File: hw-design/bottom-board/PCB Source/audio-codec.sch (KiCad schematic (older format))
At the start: 36 parts, among them U5 AP2120N-3.3, U6 CS4265, X1 24.576MHz

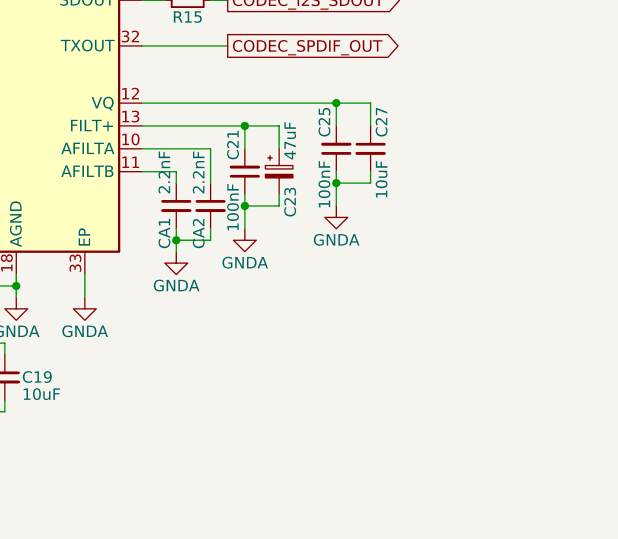
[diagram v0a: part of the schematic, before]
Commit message: change bias voltages to 5V, isolate input GND connections
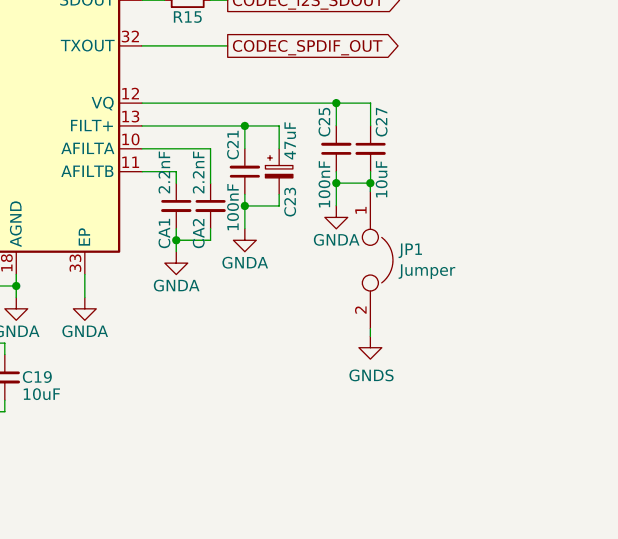
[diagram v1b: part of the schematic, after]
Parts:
- added JP1: Jumper, Jumper:SolderJumper-2_P1.3mm_Bridged_Pad1.0x1.5mm, symbol Device:Jumper
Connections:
- net GNDA: now also JP1.1
- new net GNDS: JP1.2
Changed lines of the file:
@@
 	7650 4400 7650 4450
 Wire Wire Line
-	7650 4450 7500 4450
+	7650 4450 7649 4450
 Connection ~ 7500 4450
 Wire Wire Line
@@
 Text Notes 3025 5625 0    60   ~ 0
 The series resistor at I2S_MCLK \nmust only be placed when the xtal\nis not placed, and vice versa.
+$Comp
+L power:GNDS #PWR0207
+U 1 1 5FE9F786
+P 7649 5120
+F 0 "#PWR0207" H 7649 4870 50  0001 C CNN
+F 1 "GNDS" H 7654 4947 50  0000 C CNN
+F 2 "" H 7649 5120 50  0001 C CNN
+F 3 "" H 7649 5120 50  0001 C CNN
+	1    7649 5120
+	1    0    0    -1
+$EndComp
+$Comp
+L Device:Jumper JP1
+U 1 1 5FEA81D1
+P 7649 4787
+F 0 "JP1" V 7603 4914 50  0000 L CNN
+F 1 "Jumper" V 7694 4914 50  0000 L CNN
+F 2 "Jumper:SolderJumper-2_P1.3mm_Bridged_Pad1.0x1.5mm" H 7649 4787 50  0001 C CNN
+F 3 "~" H 7649 4787 50  0001 C CNN
+	1    7649 4787
+	0    1    1    0
+$EndComp
+Wire Wire Line
+	7649 4487 7649 4450
+Connection ~ 7649 4450
+Wire Wire Line
+	7649 4450 7500 4450
+Wire Wire Line
+	7649 5087 7649 5120
 $EndSCHEMATC

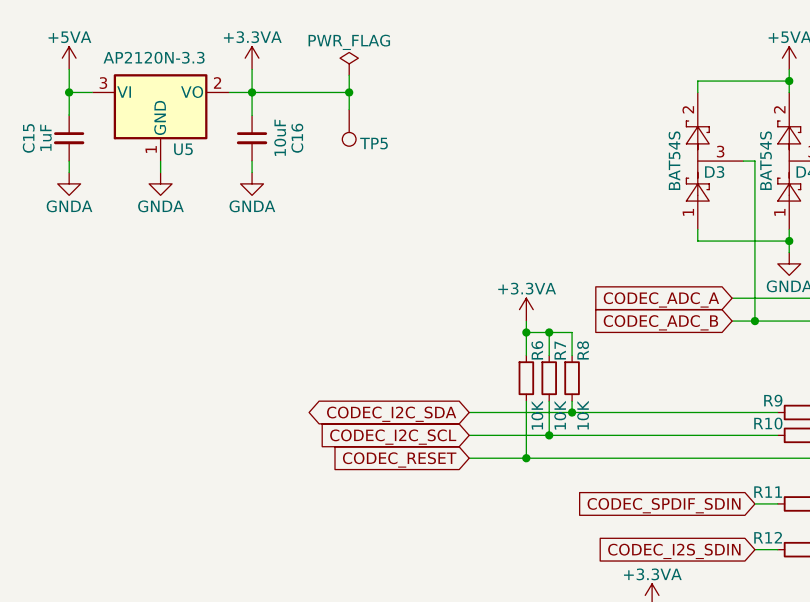
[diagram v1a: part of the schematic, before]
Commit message: add docs + change pwr schematic
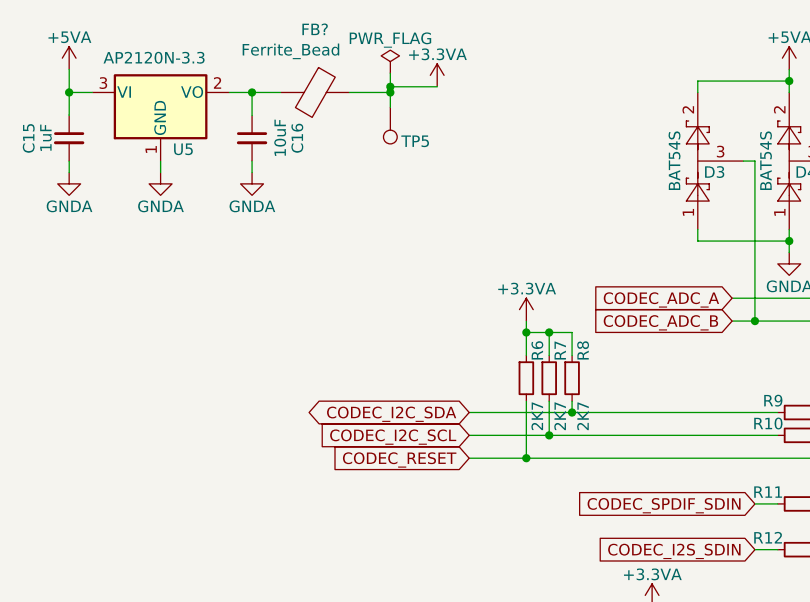
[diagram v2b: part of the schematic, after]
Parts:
- added FB?: Ferrite_Bead, symbol Device:Ferrite_Bead
- R6, R7, R8: value 10K -> 2K7; MPN RR0816P-103-D -> (none)
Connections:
- net +3.3VA: now also FB?.1; no longer C16.1, U5.2 (VO)
- new net: C16.1, FB?.2, U5.2 (VO)
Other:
- moved on the sheet: TP5
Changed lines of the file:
@@
 L bottom-board-rescue:+3.3VA-power #PWR038
 U 1 1 5B50883D
-P 2500 1950
-F 0 "#PWR038" H 2500 1800 50  0001 C CNN
-F 1 "+3.3VA" H 2500 2090 50  0000 C CNN
-F 2 "" H 2500 1950 50  0001 C CNN
-F 3 "" H 2500 1950 50  0001 C CNN
-	1    2500 1950
+P 3310 2025
+F 0 "#PWR038" H 3310 1875 50  0001 C CNN
+F 1 "+3.3VA" H 3310 2165 50  0000 C CNN
+F 2 "" H 3310 2025 50  0001 C CNN
+F 3 "" H 3310 2025 50  0001 C CNN
+	1    3310 2025
 	1    0    0    -1
 $EndComp
@@
 Connection ~ 1700 2050
 Wire Wire Line
-	2500 1950 2500 2050
-Wire Wire Line
 	2400 2050 2500 2050
-Connection ~ 2500 2050
 $Comp
 L bottom-board-rescue:GNDA-power #PWR039
@@
 L bottom-board-rescue:PWR_FLAG-power #FLG04
 U 1 1 5B621D3C
-P 2925 1975
-F 0 "#FLG04" H 2925 2050 50  0001 C CNN
-F 1 "PWR_FLAG" H 2925 2125 50  0000 C CNN
-F 2 "" H 2925 1975 50  0001 C CNN
-F 3 "~" H 2925 1975 50  0001 C CNN
-	1    2925 1975
-	1    0    0    -1
-$EndComp
-Wire Wire Line
-	2925 1975 2925 2050
-Wire Wire Line
-	2925 2050 2500 2050
+P 3105 1965
+F 0 "#FLG04" H 3105 2040 50  0001 C CNN
+F 1 "PWR_FLAG" H 3105 2115 50  0000 C CNN
+F 2 "" H 3105 1965 50  0001 C CNN
+F 3 "~" H 3105 1965 50  0001 C CNN
+	1    3105 1965
+	1    0    0    -1
+$EndComp
 $Comp
 L bottom-board-rescue:C_Small-Device C?
@@
 AR Path="/54F72B97/5B7E4010" Ref="R6"  Part="1"
 F 0 "R6" V 3750 3375 50  0000 L CNN
-F 1 "10K" V 3750 3200 50  0000 R CNN
+F 1 "2K7" V 3750 3200 50  0000 R CNN
 F 2 "Resistor_SMD:R_0603_1608Metric" H 3700 3300 60  0001 C CNN
 F 3 "" H 3700 3300 60  0000 C CNN
-F 4 "RR0816P-103-D" H 1950 -3350 50  0001 C CNN "MPN"
+F 4 "" H 1950 -3350 50  0001 C CNN "MPN"
 	1    3700 3300
 	1    0    0    -1
@@
 AR Path="/54F72B97/5B7EA59F" Ref="R7"  Part="1"
 F 0 "R7" V 3850 3375 50  0000 L CNN
-F 1 "10K" V 3850 3200 50  0000 R CNN
+F 1 "2K7" V 3850 3200 50  0000 R CNN
 F 2 "Resistor_SMD:R_0603_1608Metric" H 3800 3300 60  0001 C CNN
 F 3 "" H 3800 3300 60  0000 C CNN
-F 4 "RR0816P-103-D" H 2050 -3350 50  0001 C CNN "MPN"
+F 4 "" H 2050 -3350 50  0001 C CNN "MPN"
 	1    3800 3300
 	1    0    0    -1
@@
 AR Path="/54F72B97/5B7EA603" Ref="R8"  Part="1"
 F 0 "R8" V 3950 3375 50  0000 L CNN
-F 1 "10K" V 3950 3200 50  0000 R CNN
+F 1 "2K7" V 3950 3200 50  0000 R CNN
 F 2 "Resistor_SMD:R_0603_1608Metric" H 3900 3300 60  0001 C CNN
 F 3 "" H 3900 3300 60  0000 C CNN
-F 4 "RR0816P-103-D" H 2150 -3350 50  0001 C CNN "MPN"
 	1    3900 3300
 	1    0    0    -1
@@
 L bottom-board-rescue:TestPoint-Connector TP?
 U 1 1 5BCC4F8F
-P 2925 2125
+P 3105 2115
 AR Path="/54F7244B/5BCC4F8F" Ref="TP?"  Part="1"
 AR Path="/54F72B97/5BCC4F8F" Ref="TP5"  Part="1"
-F 0 "TP5" H 2750 2275 50  0000 L CNN
-F 1 "TestPoint" H 2983 2154 50  0001 L CNN
-F 2 "TestPoint:TestPoint_Pad_D1.0mm" H 3125 2125 50  0001 C CNN
-F 3 "~" H 3125 2125 50  0001 C CNN
-	1    2925 2125
-	-1   0    0    1
-$EndComp
-Wire Wire Line
-	2925 2125 2925 2050
-Connection ~ 2925 2050
+F 0 "TP5" H 2930 2265 50  0000 L CNN
+F 1 "TestPoint" H 3163 2144 50  0001 L CNN
+F 2 "TestPoint:TestPoint_Pad_D1.0mm" H 3305 2115 50  0001 C CNN
+F 3 "~" H 3305 2115 50  0001 C CNN
+	1    3105 2115
+	-1   0    0    1
+$EndComp
 $Comp
 L bottom-board-rescue:R_Small-Device R19
@@
 Wire Wire Line
 	7649 5087 7649 5120
+$Comp
+L Device:Ferrite_Bead FB?
+U 1 1 618FF74E
+P 2775 2050
+F 0 "FB?" V 2501 2050 50  0000 C CNN
+F 1 "Ferrite_Bead" V 2590 1945 50  0000 C CNN
+F 2 "" V 2705 2050 50  0001 C CNN
+F 3 "~" H 2775 2050 50  0001 C CNN
+	1    2775 2050
+	0    1    1    0
+$EndComp
+Wire Wire Line
+	3310 2025 3105 2025
+Wire Wire Line
+	3105 1965 3105 2025
+Wire Wire Line
+	3105 2115 3105 2050
+Connection ~ 3105 2025
+Wire Wire Line
+	2625 2050 2500 2050
+Connection ~ 2500 2050
+Wire Wire Line
+	2925 2050 3105 2050
+Wire Wire Line
+	3105 2050 3105 2025
+Connection ~ 3105 2050
+Wire Wire Line
+	3105 2050 3105 2025
 $EndSCHEMATC

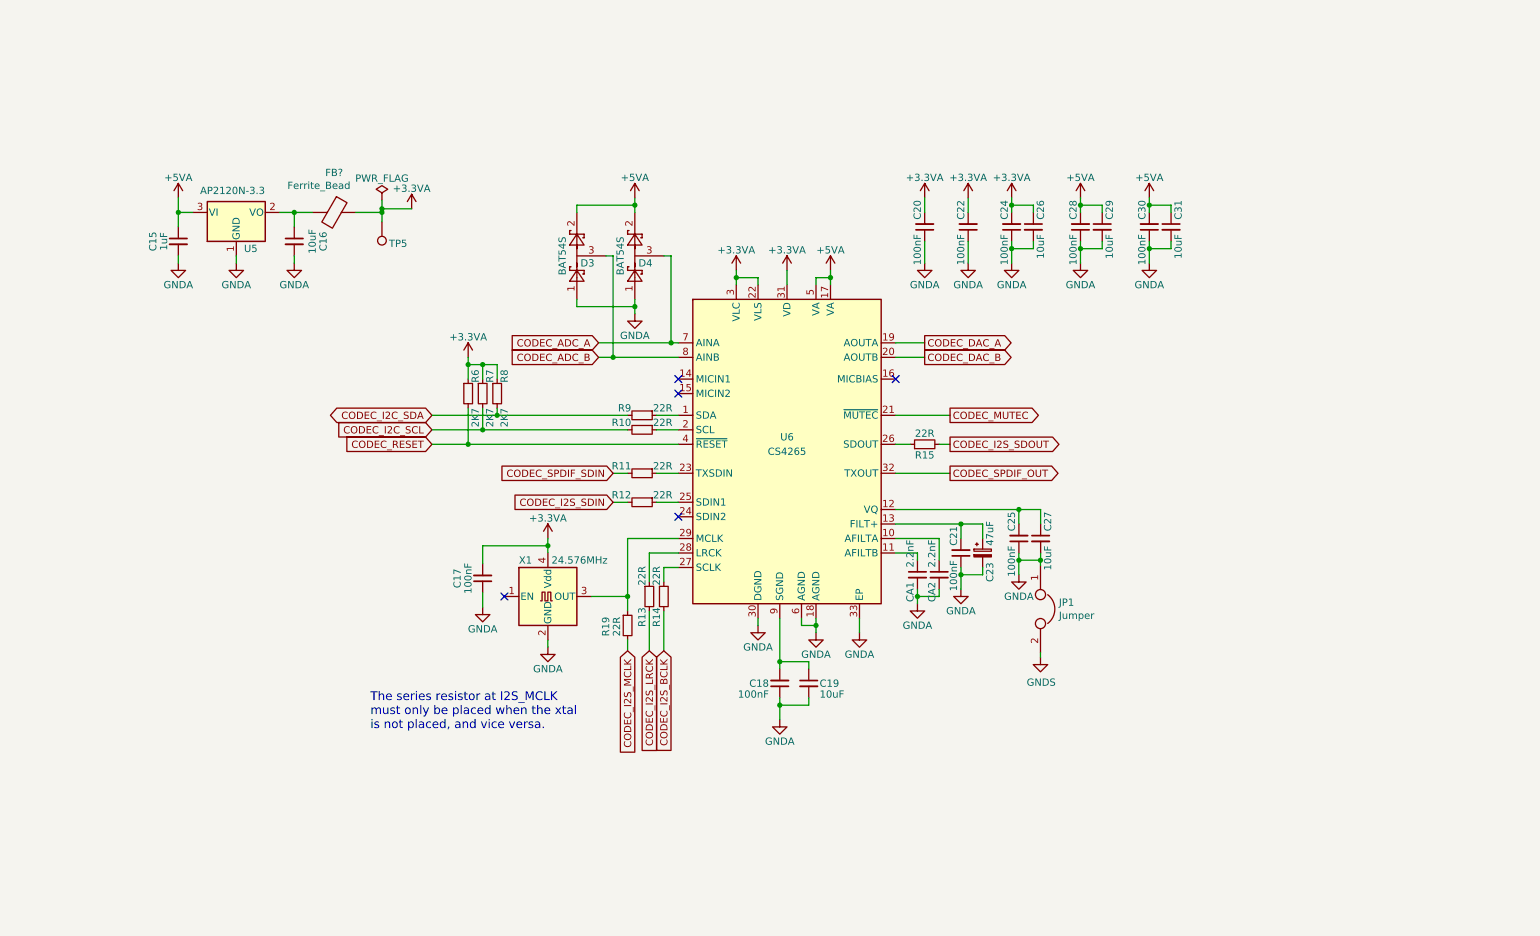
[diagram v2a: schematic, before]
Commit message: improve codec filtering
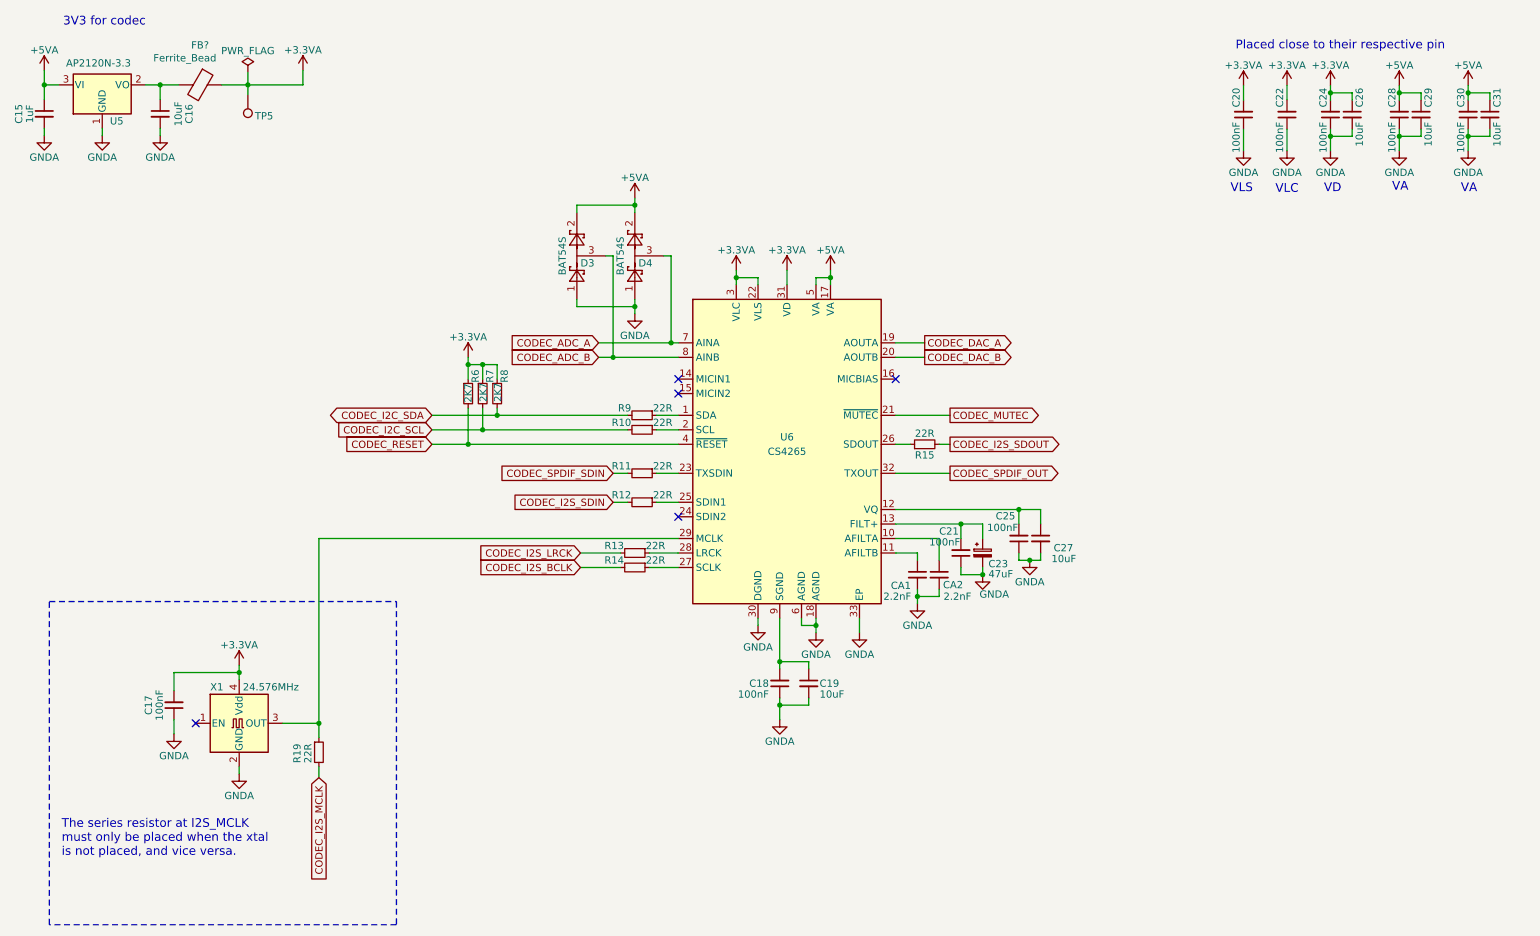
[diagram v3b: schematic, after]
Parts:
- removed JP1: Jumper, Jumper:SolderJumper-2_P1.3mm_Bridged_Pad1.0x1.5mm, symbol Device:Jumper
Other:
- note added: "3V3 for codec"
- note added: "Placed close to their respective pin"
- note added: "VA"
- note added: "VD"
- note added: "VLC"
- note added: "VLS"
- moved on the sheet: C15, C16, C17, C20, C22, C24, C26, C28, C29, C30, C31, FB?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

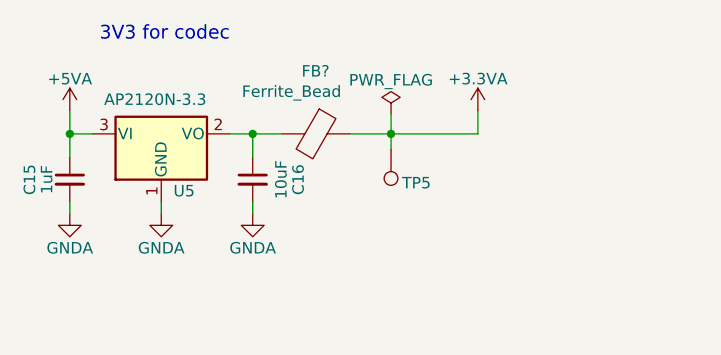
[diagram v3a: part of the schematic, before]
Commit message: place new power curcuit on the PCB
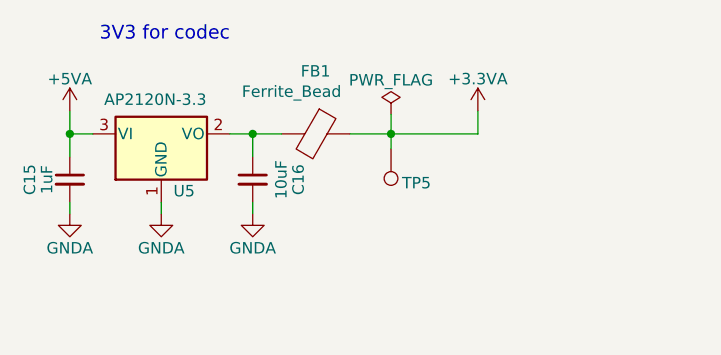
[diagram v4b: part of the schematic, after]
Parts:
- FB1: renamed from FB?; footprint (none) -> Resistor_SMD:R_0603_1608Metric; MPN (none) -> BLM18HD102SH1D
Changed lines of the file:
@@
 The series resistor at I2S_MCLK \nmust only be placed when the xtal\nis not placed, and vice versa.
 $Comp
-L Device:Ferrite_Bead FB?
+L Device:Ferrite_Bead FB1
 U 1 1 618FF74E
 P 1850 1170
-F 0 "FB?" V 1576 1170 50  0000 C CNN
+F 0 "FB1" V 1576 1170 50  0000 C CNN
 F 1 "Ferrite_Bead" V 1665 1065 50  0000 C CNN
-F 2 "" V 1780 1170 50  0001 C CNN
+F 2 "Resistor_SMD:R_0603_1608Metric" V 1780 1170 50  0001 C CNN
 F 3 "~" H 1850 1170 50  0001 C CNN
+F 4 "BLM18HD102SH1D" V 1850 1170 50  0001 C CNN "MPN"
 	1    1850 1170
 	0    1    1    0
@@
 	7575 4450 7650 4450
 $Comp
-L bottom-board-rescue:GNDA-power #PWR?
+L bottom-board-rescue:GNDA-power #PWR0184
 U 1 1 618DBE7A
 P 7250 4550
-F 0 "#PWR?" H 7250 4300 50  0001 C CNN
+F 0 "#PWR0184" H 7250 4300 50  0001 C CNN
 F 1 "GNDA" H 7330 4415 50  0000 C CNN
 F 2 "" H 7250 4550 60  0000 C CNN

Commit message: update all MPN's to match the Dwarf
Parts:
- C15: MPN CL10B105KP8NNNC -> TMK107B7105KA-T
- C16, C19, C26, C27, C29, C31: footprint Capacitor_SMD:C_0603_1608Metric -> Capacitor_SMD:C_0805_2012Metric; MPN CL10A106MQ8NNNC -> GRM219R61E106KA12D
- R6, R7, R8: MPN (none) -> CRGCQ0603F2K7
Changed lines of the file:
@@
 Sheet 3 13
 Title "MOD DuoX - Bottom Board"
-Date "2020-05-15"
-Rev "Rev 1.12"
+Date "2021-11-11"
+Rev "Rev 1.05"
 Comp "MOD Devices GmbH"
 Comment1 "DuoX Audio processing board"
 Comment2 "https://github.com/moddevices/mod-hw-duoX"
-Comment3 ""
-Comment4 ""
+Comment3 "Inp Power: 12V 700mA"
+Comment4 "USB outp Power: 500mA"
 $EndDescr
 $Comp
@@
 F 2 "Capacitor_SMD:C_0603_1608Metric" H 775 1370 60  0001 C CNN
 F 3 "" H 775 1370 60  0000 C CNN
-F 4 "CL10B105KP8NNNC" H -3425 370 50  0001 C CNN "MPN"
+F 4 "TMK107B7105KA-T" H -3425 370 50  0001 C CNN "MPN"
 	1    775  1370
 	-1   0    0    -1
@@
 F 0 "C16" V 1375 1370 50  0000 C CNN
 F 1 "10uF" V 1450 1370 50  0000 C CNN
-F 2 "Capacitor_SMD:C_0603_1608Metric" H 1575 1370 60  0001 C CNN
+F 2 "Capacitor_SMD:C_0805_2012Metric" H 1575 1370 60  0001 C CNN
 F 3 "" H 1575 1370 60  0000 C CNN
-F 4 "CL10A106MQ8NNNC" H -3725 -3980 50  0001 C CNN "MPN"
+F 4 "GRM219R61E106KA12D" H -3725 -3980 50  0001 C CNN "MPN"
 	1    1575 1370
 	-1   0    0    -1
@@
 F 0 "C26" V 9750 1425 50  0000 L CNN
 F 1 "10uF" V 9750 1325 50  0000 R CNN
-F 2 "Capacitor_SMD:C_0603_1608Metric" H 9800 1375 60  0001 C CNN
+F 2 "Capacitor_SMD:C_0805_2012Metric" H 9800 1375 60  0001 C CNN
 F 3 "" H 9800 1375 60  0000 C CNN
-F 4 "CL10A106MQ8NNNC" H 4500 -3975 50  0001 C CNN "MPN"
+F 4 "GRM219R61E106KA12D" H 4500 -3975 50  0001 C CNN "MPN"
 	1    9800 1375
 	-1   0    0    -1
@@
 F 0 "C29" V 10225 1425 50  0000 L CNN
 F 1 "10uF" V 10225 1325 50  0000 R CNN
-F 2 "Capacitor_SMD:C_0603_1608Metric" H 10275 1375 60  0001 C CNN
+F 2 "Capacitor_SMD:C_0805_2012Metric" H 10275 1375 60  0001 C CNN
 F 3 "" H 10275 1375 60  0000 C CNN
-F 4 "CL10A106MQ8NNNC" H 4975 -3975 50  0001 C CNN "MPN"
+F 4 "GRM219R61E106KA12D" H 4975 -3975 50  0001 C CNN "MPN"
 	1    10275 1375
 	-1   0    0    -1
@@
 F 0 "C31" V 10700 1425 50  0000 L CNN
 F 1 "10uF" V 10700 1325 50  0000 R CNN
-F 2 "Capacitor_SMD:C_0603_1608Metric" H 10750 1375 60  0001 C CNN
+F 2 "Capacitor_SMD:C_0805_2012Metric" H 10750 1375 60  0001 C CNN
 F 3 "" H 10750 1375 60  0000 C CNN
-F 4 "CL10A106MQ8NNNC" H 5450 -3975 50  0001 C CNN "MPN"
+F 4 "GRM219R61E106KA12D" H 5450 -3975 50  0001 C CNN "MPN"
 	1    10750 1375
 	-1   0    0    -1
@@
 F 0 "C19" H 5975 5300 50  0000 R CNN
 F 1 "10uF" H 5975 5225 50  0000 R CNN
-F 2 "Capacitor_SMD:C_0603_1608Metric" H 6050 5300 60  0001 C CNN
+F 2 "Capacitor_SMD:C_0805_2012Metric" H 6050 5300 60  0001 C CNN
 F 3 "" H 6050 5300 60  0000 C CNN
-F 4 "CL10A106MQ8NNNC" H 750 -50 50  0001 C CNN "MPN"
+F 4 "GRM219R61E106KA12D" H 750 -50 50  0001 C CNN "MPN"
 	1    6050 5300
 	-1   0    0    -1
@@
 F 2 "Resistor_SMD:R_0603_1608Metric" H 3700 3300 60  0001 C CNN
 F 3 "" H 3700 3300 60  0000 C CNN
-F 4 "" H 1950 -3350 50  0001 C CNN "MPN"
+F 4 "CRGCQ0603F2K7" H 1950 -3350 50  0001 C CNN "MPN"
 	1    3700 3300
 	1    0    0    -1
@@
 F 2 "Resistor_SMD:R_0603_1608Metric" H 3800 3300 60  0001 C CNN
 F 3 "" H 3800 3300 60  0000 C CNN
-F 4 "" H 2050 -3350 50  0001 C CNN "MPN"
+F 4 "CRGCQ0603F2K7" H 2050 -3350 50  0001 C CNN "MPN"
 	1    3800 3300
 	1    0    0    -1
@@
 F 2 "Resistor_SMD:R_0603_1608Metric" H 3900 3300 60  0001 C CNN
 F 3 "" H 3900 3300 60  0000 C CNN
+F 4 "CRGCQ0603F2K7" V 3900 3300 50  0001 C CNN "MPN"
 	1    3900 3300
 	1    0    0    -1
@@
 F 0 "C27" H 7425 4235 50  0000 L CNN
 F 1 "10uF" H 7575 4160 50  0000 R CNN
-F 2 "Capacitor_SMD:C_0603_1608Metric" H 7650 4300 60  0001 C CNN
+F 2 "Capacitor_SMD:C_0805_2012Metric" H 7650 4300 60  0001 C CNN
 F 3 "" H 7650 4300 60  0000 C CNN
-F 4 "CL10A106MQ8NNNC" H 2350 -1050 50  0001 C CNN "MPN"
+F 4 "GRM219R61E106KA12D" H 2350 -1050 50  0001 C CNN "MPN"
 	1    7650 4300
 	-1   0    0    -1
